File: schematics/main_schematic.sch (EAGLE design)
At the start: 1 part

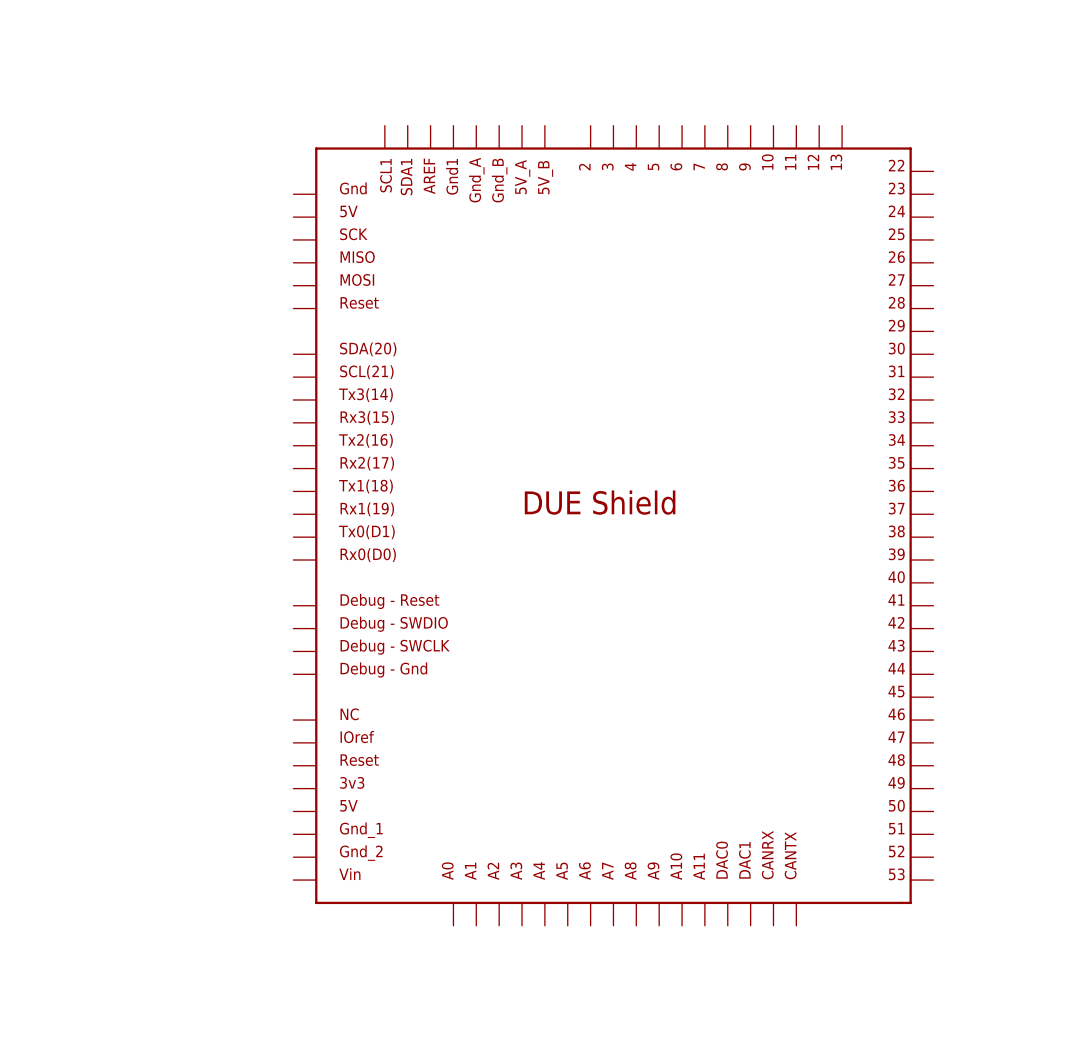
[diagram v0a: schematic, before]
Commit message: Arduino DUE Labeled compatibile with Due3Dom
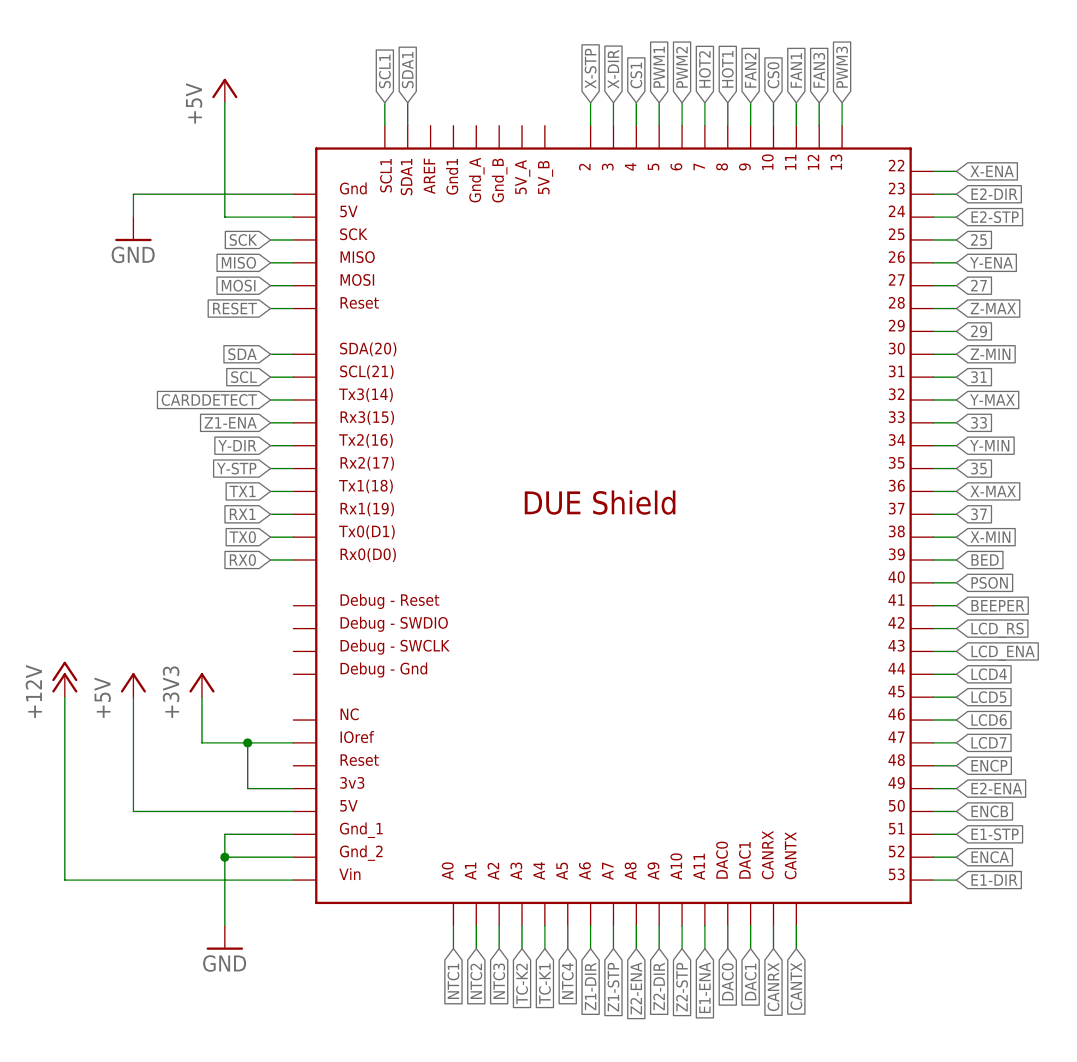
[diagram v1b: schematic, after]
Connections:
- new net +12V: U$1.VIN
- new net +3V3: U$1.3V3, U$1.IOREF
- new net +5V: U$1.5V, U$1.GND_ICSP
- new net 25: U$1.25
- new net 27: U$1.27
- new net 29: U$1.29
- new net 31: U$1.31
- new net 33: U$1.33
- new net 35: U$1.35
- new net 37: U$1.37
- new net BED: U$1.39
- new net BEEPER: U$1.41
- new net CANRX: U$1.CANRX
- new net CANTX: U$1.CANTX
- new net CARDDETECT: U$1.TX3
- new net CS0: U$1.10
- new net CS1: U$1.4
- new net DAC0: U$1.DAC0
- new net DAC1: U$1.DAC1
- new net E1-DIR: U$1.53
- new net E1-ENA: U$1.A11
- new net E1-STP: U$1.51
- new net E2-DIR: U$1.23
- new net E2-ENA: U$1.49
- new net E2-STP: U$1.24
- new net ENCA: U$1.52
- new net ENCB: U$1.50
- new net ENCP: U$1.48
- new net FAN1: U$1.11
- new net FAN2: U$1.9
- new net FAN3: U$1.12
- new net GND: U$1.5V_ICSP, U$1.GND_1, U$1.GND_2
- new net HOT1: U$1.8
- new net HOT2: U$1.7
- new net LCD4: U$1.44
- new net LCD5: U$1.45
- new net LCD6: U$1.46
- new net LCD7: U$1.47
- new net LCD_ENA: U$1.43
- new net LCD_RS: U$1.42
- new net MISO: U$1.MISO_ICSP
- new net MOSI: U$1.MOSI_ICSP
- new net NTC1: U$1.A0
- new net NTC2: U$1.A1
- new net NTC3: U$1.A2
- new net NTC4: U$1.A5
- new net PSON: U$1.40
- new net PWM1: U$1.5
- new net PWM2: U$1.6
- new net PWM3: U$1.13
- new net RESET: U$1.RESET_ICSP
- new net RX0: U$1.RX0
- new net RX1: U$1.RX1
- new net SCK: U$1.SCK_ICSP
- new net SCL: U$1.SCL
- new net SCL1: U$1.SCL1
- new net SDA: U$1.SDA
- new net SDA1: U$1.SDA1
- new net TC-K1: U$1.A4
- new net TC-K2: U$1.A3
- new net TX0: U$1.TX0
- new net TX1: U$1.TX1
- new net X-DIR: U$1.3
- new net X-ENA: U$1.22
- new net X-MAX: U$1.36
- new net X-MIN: U$1.38
- new net X-STP: U$1.2
- new net Y-DIR: U$1.TX2
- new net Y-ENA: U$1.26
- new net Y-MAX: U$1.32
- new net Y-MIN: U$1.34
- new net Y-STP: U$1.RX2
- new net Z-MAX: U$1.28
- new net Z-MIN: U$1.30
- new net Z1-DIR: U$1.A6
- new net Z1-ENA: U$1.RX3
- new net Z1-STP: U$1.A7
- new net Z2-DIR: U$1.A9
- new net Z2-ENA: U$1.A8
- new net Z2-STP: U$1.A10

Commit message: Endstops added
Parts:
- added C1, C2, C3, C4, C5, C6: 100nF, resistor:C-EUC0805
- added C7, C8: (no value), resistor:C-EUC0805
- added R1, R2, R3, R4, R5, R6: 10K, resistor:R-EU_R0805
- added XMAX: X-MAX, Rembrandt Electronics - JST XH Connectors v1-0:JST-XH-03-PIN-LONG-PAD
- added XMIN: X-MIN, Rembrandt Electronics - JST XH Connectors v1-0:JST-XH-03-PIN-LONG-PAD
- added YMAX: Y-MAX, Rembrandt Electronics - JST XH Connectors v1-0:JST-XH-03-PIN-LONG-PAD
- added YMIN: Y-MIN, Rembrandt Electronics - JST XH Connectors v1-0:JST-XH-03-PIN-LONG-PAD
- added ZMAX: Z-MAX, Rembrandt Electronics - JST XH Connectors v1-0:JST-XH-03-PIN-LONG-PAD
- added ZMIN: Z-MIN, Rembrandt Electronics - JST XH Connectors v1-0:JST-XH-03-PIN-LONG-PAD
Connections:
- new net X-MAX-OUT: R2.1, XMAX-3.S
- new net X-MIN-OUT: R1.1, XMIN-3.S
- new net Y-MAX-OUT: R4.1, YMAX-3.S
- new net Y-MIN-OUT: R3.1, YMIN-3.S
- new net Z-MAX-OUT: R6.1, ZMAX-3.S
- new net Z-MIN-OUT: R5.1, ZMIN-3.S
- net +5V: now also C7.1, C8.1, XMAX-2.S, XMIN-2.S, YMAX-2.S, YMIN-2.S, ZMAX-2.S, ZMIN-2.S
- net GND: now also C1.2, C2.2, C3.2, C4.2, C5.2, C6.2, C7.2, C8.2, XMAX-1.S, XMIN-1.S, YMAX-1.S, YMIN-1.S, ZMAX-1.S, ZMIN-1.S
- net X-MAX: now also C2.1, R2.2
- net X-MIN: now also C1.1, R1.2
- net Y-MAX: now also C4.1, R4.2
- net Y-MIN: now also C3.1, R3.2
- net Z-MAX: now also C6.1, R6.2
- net Z-MIN: now also C5.1, R5.2

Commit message: Fans sheet created
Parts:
- added LED1, LED2, LED3: (no value), led:LEDSMT1206
- added Q1, Q2, Q3: IRLML0030TRPBF, fets:MOSFET-NCHANNELSMD
- added R10, R13, R7: 2K7, resistor:R-EU_R0805
- added R11, R14, R8: 100R, resistor:R-EU_R0805
- added R12, R15, R9: 10K, resistor:R-EU_R0805
- added SV1, SV2, SV3: (no value), con-lstb:MA03-2
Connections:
- new net +24V: SV1.6, SV2.6, SV3.6
- new net FAN1+: R7.1, SV1.1, SV1.3, SV1.5
- new net FAN1-: LED1.C, Q1.D
- new net FAN2+: R10.1, SV2.1, SV2.3, SV2.5
- new net FAN2-: LED2.C, Q2.D
- new net FAN3+: R13.1, SV3.1, SV3.3, SV3.5
- new net FAN3-: LED3.C, Q3.D
- new net N$1: LED3.A, R13.2
- new net N$2: LED1.A, R7.2
- new net N$3: LED2.A, R10.2
- new net N$4: Q2.G, R11.2, R12.1
- new net N$5: Q1.G, R8.2, R9.1
- new net N$6: Q3.G, R14.2, R15.1
- net +12V: now also SV1.4, SV2.4, SV3.4
- net +5V: now also SV1.2, SV2.2, SV3.2
- net FAN1: now also R8.1
- net FAN2: now also R11.1
- net FAN3: now also R14.1
- net GND: now also Q1.S, Q2.S, Q3.S, R12.2, R15.2, R9.2

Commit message: Fan connectors added
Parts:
- added FAN1: FAN1, Rembrandt Electronics - JST XH Connectors v1-0:JST-XH-03-PIN-LONG-PAD
- added FAN2: FAN2, Rembrandt Electronics - JST XH Connectors v1-0:JST-XH-03-PIN-LONG-PAD
- added FAN3: FAN3, Rembrandt Electronics - JST XH Connectors v1-0:JST-XH-03-PIN-LONG-PAD
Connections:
- net FAN1+: now also FAN1-2.S
- net FAN1-: now also FAN1-3.S
- net FAN2+: now also FAN2-2.S
- net FAN2-: now also FAN2-3.S
- net FAN3+: now also FAN3-2.S
- net FAN3-: now also FAN3-3.S
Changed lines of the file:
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@@
 <part name="SV3" library="con-lstb" library_urn="urn:adsk.eagle:library:162" deviceset="MA03-2" device="" package3d_urn="urn:adsk.eagle:package:8334/1"/>
 <part name="GND9" library="supply1" library_urn="urn:adsk.eagle:library:371" deviceset="GND" device=""/>
+<part name="FAN1" library="Rembrandt Electronics - JST XH Connectors v1-0" deviceset="JST-XH-03-PIN" device="-LONG-PAD" value="FAN1"/>
+<part name="FAN2" library="Rembrandt Electronics - JST XH Connectors v1-0" deviceset="JST-XH-03-PIN" device="-LONG-PAD" value="FAN2"/>
+<part name="FAN3" library="Rembrandt Electronics - JST XH Connectors v1-0" deviceset="JST-XH-03-PIN" device="-LONG-PAD" value="FAN3"/>
 </parts>
 <sheets>
@@
 </plain>
 <instances>
+<instance part="FAN1" gate="-1" x="17.78" y="76.2" rot="R180"/>
+<instance part="FAN1" gate="-2" x="17.78" y="78.74" rot="R180"/>
+<instance part="FAN1" gate="-3" x="17.78" y="81.28" rot="R180"/>
+<instance part="FAN2" gate="-1" x="17.78" y="58.42" rot="R180"/>
+<instance part="FAN2" gate="-2" x="17.78" y="60.96" rot="R180"/>
+<instance part="FAN2" gate="-3" x="17.78" y="63.5" rot="R180"/>
+<instance part="FAN3" gate="-1" x="17.78" y="38.1" rot="R180"/>
+<instance part="FAN3" gate="-2" x="17.78" y="40.64" rot="R180"/>
+<instance part="FAN3" gate="-3" x="17.78" y="43.18" rot="R180"/>
 </instances>
 <busses>
 </busses>
 <nets>
+<net name="FAN1-" class="0">
+<segment>
+<pinref part="FAN1" gate="-3" pin="S"/>
+<wire x1="20.32" y1="81.28" x2="22.86" y2="81.28" width="0.1524" layer="91"/>
+<label x="22.86" y="81.28" size="1.27" layer="95" xref="yes"/>
+</segment>
+</net>
+<net name="FAN1+" class="0">
+<segment>
+<pinref part="FAN1" gate="-2" pin="S"/>
+<wire x1="20.32" y1="78.74" x2="22.86" y2="78.74" width="0.1524" layer="91"/>
+<label x="22.86" y="78.74" size="1.27" layer="95" xref="yes"/>
+</segment>
+</net>
+<net name="FAN2+" class="0">
+<segment>
+<pinref part="FAN2" gate="-2" pin="S"/>
+<wire x1="20.32" y1="60.96" x2="22.86" y2="60.96" width="0.1524" layer="91"/>
+<label x="22.86" y="60.96" size="1.27" layer="95" xref="yes"/>
+</segment>
+</net>
+<net name="FAN3-" class="0">
+<segment>
+<pinref part="FAN3" gate="-3" pin="S"/>
+<wire x1="20.32" y1="43.18" x2="22.86" y2="43.18" width="0.1524" layer="91"/>
+<label x="22.86" y="43.18" size="1.27" layer="95" xref="yes"/>
+</segment>
+</net>
+<net name="FAN3+" class="0">
+<segment>
+<pinref part="FAN3" gate="-2" pin="S"/>
+<wire x1="20.32" y1="40.64" x2="22.86" y2="40.64" width="0.1524" layer="91"/>
+<label x="22.86" y="40.64" size="1.27" layer="95" xref="yes"/>
+</segment>
+</net>
+<net name="FAN2-" class="0">
+<segment>
+<pinref part="FAN2" gate="-3" pin="S"/>
+<wire x1="20.32" y1="63.5" x2="22.86" y2="63.5" width="0.1524" layer="91"/>
+<label x="22.86" y="63.5" size="1.27" layer="95" xref="yes"/>
+</segment>
+</net>
 </nets>
 </sheet>

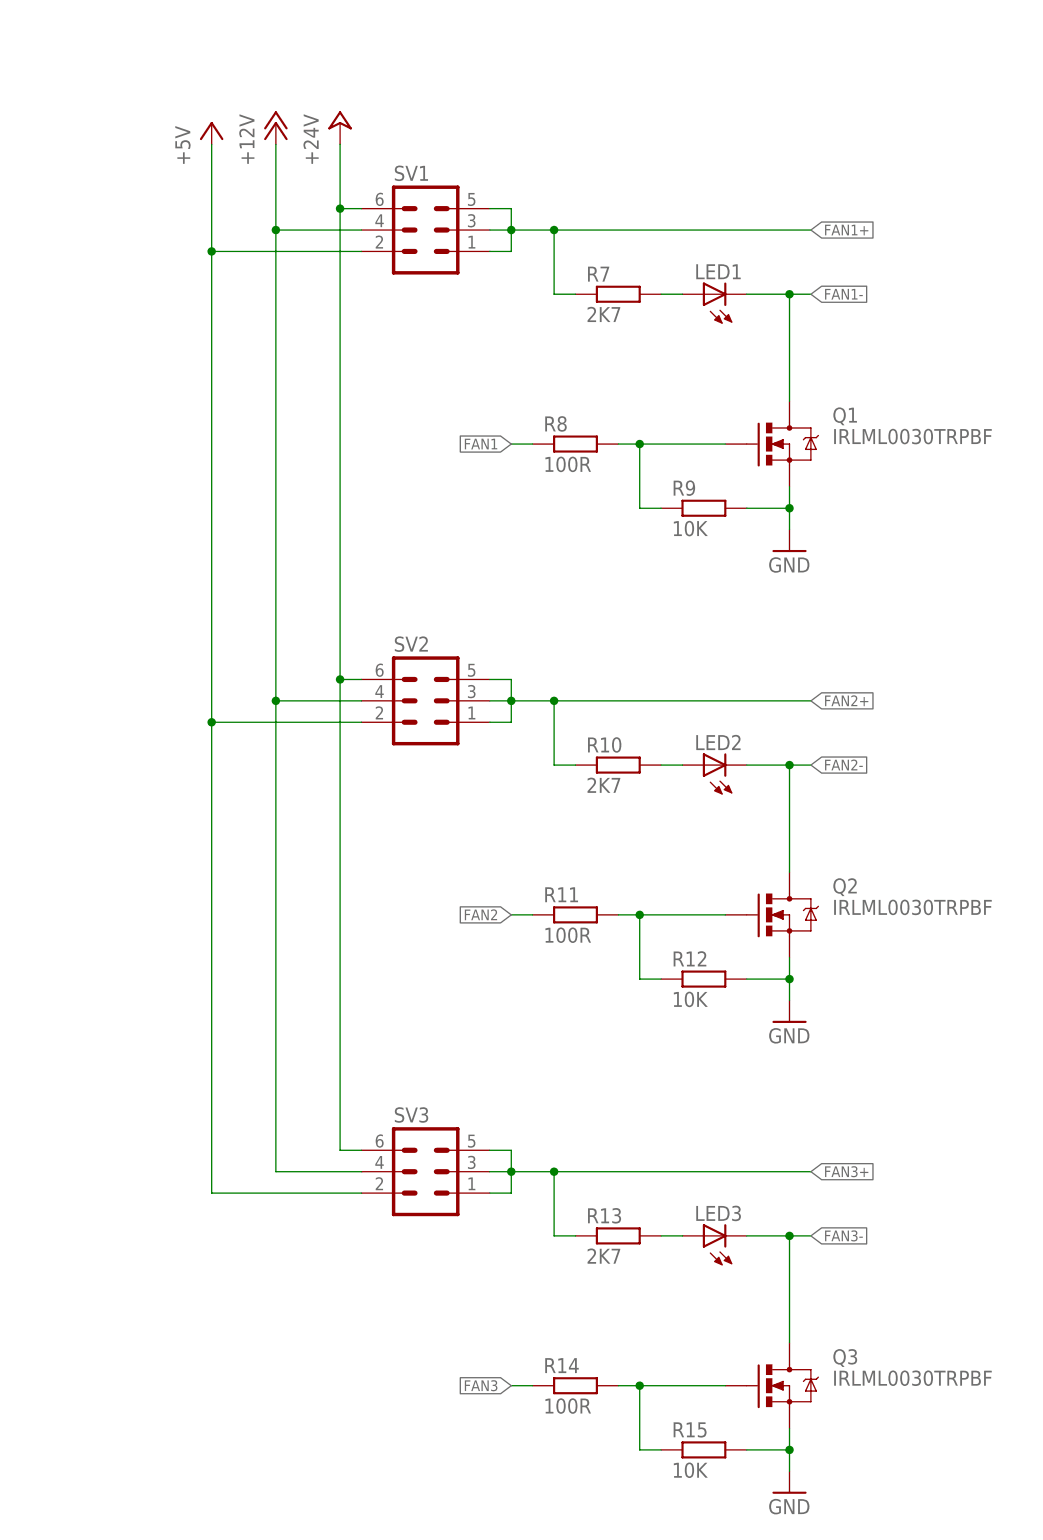
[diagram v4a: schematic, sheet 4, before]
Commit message: Fan jumpers fixed
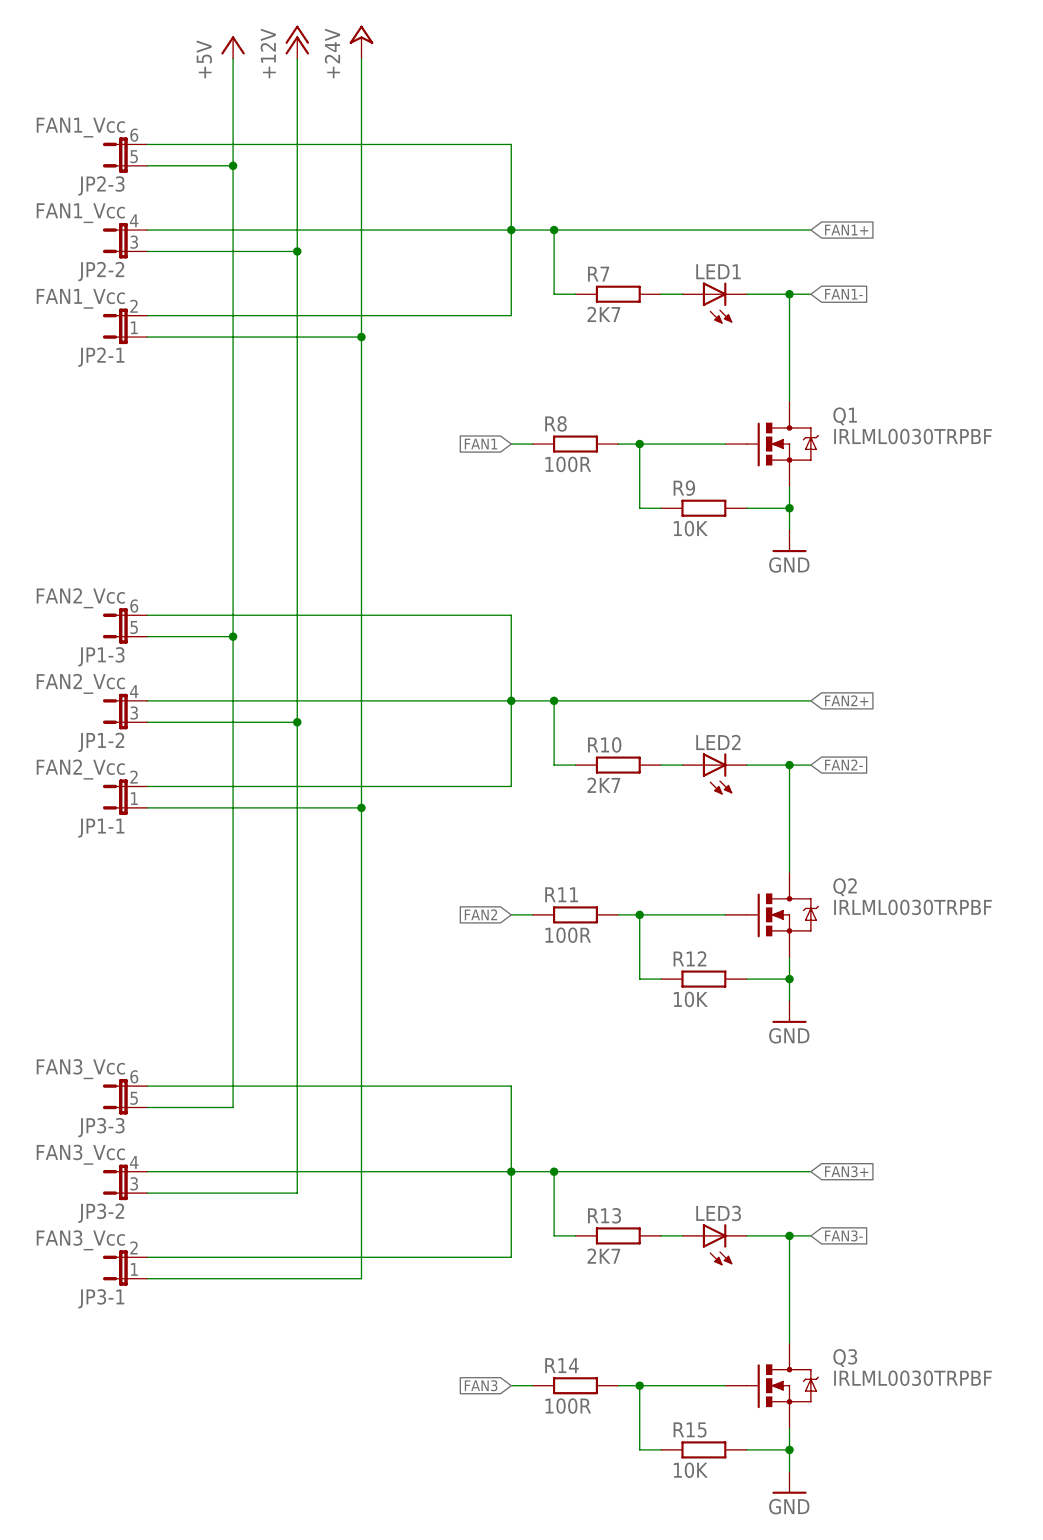
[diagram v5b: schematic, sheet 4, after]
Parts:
- removed SV1, SV2, SV3: (no value), con-lstb:MA03-2
- added JP1: FAN2_Vcc, jumper:JP3QE
- added JP2: FAN1_Vcc, jumper:JP3QE
- added JP3: FAN3_Vcc, jumper:JP3QE
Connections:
- net +12V: now also JP1-2.1, JP2-2.1, JP3-2.1; no longer SV1.4, SV2.4, SV3.4
- net +24V: now also JP1-1.1, JP2-1.1, JP3-1.1; no longer SV1.6, SV2.6, SV3.6
- net +5V: now also JP1-3.1, JP2-3.1, JP3-3.1; no longer SV1.2, SV2.2, SV3.2
- net FAN1+: now also JP2-1.2, JP2-2.2, JP2-3.2; no longer SV1.1, SV1.3, SV1.5
- net FAN2+: now also JP1-1.2, JP1-2.2, JP1-3.2; no longer SV2.1, SV2.3, SV2.5
- net FAN3+: now also JP3-1.2, JP3-2.2, JP3-3.2; no longer SV3.1, SV3.3, SV3.5
